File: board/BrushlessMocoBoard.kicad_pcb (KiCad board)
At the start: 2 copper layers, 127 x 127 mm, 116 parts, among them J5 Conn_01x04, Q1 NMOS, Q2 NMOS, Q3 NMOS, Q4 NMOS, Q7 NMOS, Q8 NMOS, SW1 SW_Push, U1 STSPIN32G4TR, U2 SN65HVD232

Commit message: Adjusted diode footprints and grouped layout components
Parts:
- CR1, CR2, CR3, CR4, CR7, CR8: footprint BoCoFootprintLibrary:DO-35_STM -> Diode_THT:D_DO-35_SOD27_P3.81mm_Vertical_KathodeUp
- moved C24 344.5 mm to (267.0, 57.9)
- moved C26 343.5 mm to (251.0, 58.2)
- moved Q3 333.1 mm to (270.2, 70.5)
- moved Q4 333.1 mm to (270.2, 77.2)
- moved R10 313.8 mm to (248.3, 91.5)
- moved R8 313.8 mm to (248.3, 86.4)
- moved R9 313.8 mm to (248.3, 89.0)
- moved C3 313.4 mm to (248.3, 81.9)
- moved TP3 308.8 mm to (257.2, 108.9)
- moved R50 307.6 mm to (259.9, 83.4)
- moved R51 307.6 mm to (259.9, 85.9)
- moved R52 307.6 mm to (259.9, 88.4)
- moved R53 307.6 mm to (259.9, 90.9)
- moved C8 306.7 mm to (229.9, 59.0), turned to 180 degrees
- moved R31 306.5 mm to (249.8, 110.1)
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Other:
- board outline removed

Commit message: Placed some basic planes in the layout and swapped mosfet symbols to match layout footprints.
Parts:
- removed C25, C26: 330 μF, BoCoFootprintLibrary:CAP_PAN_EEE_H13_PAN
- removed CR7, CR8: BAT48, Diode_THT:D_DO-35_SOD27_P3.81mm_Vertical_KathodeUp
- removed Q1, Q2, Q3, Q4, Q7, Q8: NMOS, BoCoFootprintLibrary:PG-TDSON-8_INF
- added C10: 1 µF / 25 V, Capacitor_SMD:C_0603_1608Metric_Pad1.08x0.95mm_HandSolder, F.Cu at (225.0, 72.4)
- added C13 (x2): 10 μF / 25 V, BrushlessMocoBoard:CAPPRD250W45D400H700, F.Cu at (2.89, 2.21)
- added C5: 1 mF, Capacitor_THT:CP_Radial_D12.5mm_P5.00mm, F.Cu at (180.0, 110.6)
- added CR5: BAT48, Diode_THT:D_DO-35_SOD27_P3.81mm_Vertical_KathodeUp, F.Cu at (204.9, 64.1)
- added CR6: BAT48, Diode_THT:D_DO-35_SOD27_P3.81mm_Vertical_KathodeUp, F.Cu at (205.1, 76.2)
- added MOSFET1: BSC035N10NS5ATMA1, BoCoFootprintLibrary:PG-TDSON-8_INF, F.Cu at (120.9, 93.3)
- added MOSFET2: BSC035N10NS5ATMA1, BoCoFootprintLibrary:PG-TDSON-8_INF, F.Cu at (135.9, 93.3)
- added MOSFET3: BSC035N10NS5ATMA1, BoCoFootprintLibrary:PG-TDSON-8_INF, F.Cu at (165.0, 93.7)
- added MOSFET4: BSC035N10NS5ATMA1, BoCoFootprintLibrary:PG-TDSON-8_INF, F.Cu at (180.0, 93.7)
- added MOSFET5: BSC035N10NS5ATMA1, BoCoFootprintLibrary:PG-TDSON-8_INF, F.Cu at (208.9, 93.6)
- added MOSFET6: BSC035N10NS5ATMA1, BoCoFootprintLibrary:PG-TDSON-8_INF, F.Cu at (224.2, 93.6)
- added R11: 47 Ω, Resistor_SMD:R_0603_1608Metric_Pad0.98x0.95mm_HandSolder, F.Cu at (174.6, 80.0)
- added R12: 10 Ω, Resistor_SMD:R_0603_1608Metric_Pad0.98x0.95mm_HandSolder, F.Cu at (168.9, 65.4)
- added R13: 10 Ω, Resistor_SMD:R_0603_1608Metric_Pad0.98x0.95mm_HandSolder, F.Cu at (170.2, 80.0)
- C12: value 1 µF / 25 V -> 1 mF; footprint Capacitor_SMD:C_0603_1608Metric_Pad1.08x0.95mm_HandSolder -> Capacitor_THT:CP_Radial_D12.5mm_P5.00mm
- C24, C8: value 1 mF -> 330 μF; footprint Capacitor_THT:CP_Radial_D12.5mm_P5.00mm -> BoCoFootprintLibrary:CAP_PAN_EEE_H13_PAN
- R43, R50: value 47 Ω -> 1 mΩ / 1%
- R44, R47: value 10 Ω -> 47 Ω
- R46: value 47 Ω -> 10 Ω
- R49: value 1 mΩ / 1% -> 10 Ω
- R51, R52: value 10 Ω -> 0 Ω
- R53: value 1 mΩ / 1% -> 0 Ω
- moved R51 271.9 mm to (1.68, 0.76)
- moved R52 271.9 mm to (1.68, 3.27)
- moved R53 271.9 mm to (1.68, 5.78)
- moved C19 193.5 mm to (168.2, 240.6)
- moved C20 193.5 mm to (172.1, 259.7)
- moved R17 193.5 mm to (172.6, 243.1)
- moved R18 193.5 mm to (167.5, 258.0)
- moved R19 193.5 mm to (167.5, 260.5)
- moved R5 193.5 mm to (163.2, 258.0)
- moved R7 193.5 mm to (163.2, 260.5)
- moved SW1 193.5 mm to (171.2, 247.4)
- moved Conn4 161.9 mm to (57.9, 206.0)
- moved Conn8 161.9 mm to (57.9, 218.1)
- moved TP1 161.1 mm to (320.7, 170.4)
- moved TP4 161.1 mm to (320.8, 177.3)
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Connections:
- C11 pad 2: Vs_U_Low -> GND
- C12 pad 1: /Half-Bridges & Current Sensing/BOOT_V -> 24 V
- C12 pad 2: /Half-Bridges & Current Sensing/OUT_V -> GND
- C14 pad 2: Vs_U_Low -> GND
- C15 pad 2: Vs_U_Low -> GND
- C16 pad 2: Vs_U_Low -> GND
- C17 pad 2: Vs_U_Low -> GND
- C18 pad 2: Vs_U_Low -> GND
- C19 pad 2: Vs_U_Low -> GND
- C2 pad 2: Vs_U_Low -> GND
- C20 pad 2: Vs_U_Low -> GND
- C21 pad 2: Vs_U_Low -> GND
- C22 pad 2: Vs_U_Low -> GND
- C23 pad 2: Vs_U_Low -> GND
- C24 pad 2: Vs_U_Low -> GND
- C3 pad 1: /Half-Bridges & Current Sensing/BOOT_W -> /Half-Bridges & Current Sensing/BOOT_V
- C3 pad 2: /Half-Bridges & Current Sensing/OUT_W -> /Half-Bridges & Current Sensing/OUT_V
- C4 pad 2: Vs_U_Low -> GND
- C6 pad 2: Vs_U_Low -> GND
- C7 pad 2: Vs_U_Low -> GND
- C8 pad 2: Vs_U_Low -> GND
- C9 pad 2: Vs_U_Low -> GND
- CR3 pad 1: /Half-Bridges & Current Sensing/GHS_W -> /Half-Bridges & Current Sensing/GHS_V
- CR3 pad 2: Net-(Q3-G) -> Net-(CR3-Pad2)
- CR4 pad 1: /Half-Bridges & Current Sensing/GLS_W -> /Half-Bridges & Current Sensing/GLS_V
- CR4 pad 2: Net-(Q4-G) -> Net-(CR4-Pad2)
- Conn1 pad 1: Vs_U_Low -> GND
- Conn4 pad 4: Vs_U_Low -> GND
- D1 pad 1: Vs_U_Low -> GND
- D3 pad 1: Vs_U_Low -> GND
- J5 pad 1: +3V3 -> +3.3V
- J5 pad 4: Vs_U_Low -> GND
- R10 pad 1: /Half-Bridges & Current Sensing/GLS_W -> /Half-Bridges & Current Sensing/GLS_V
- R16 pad 2: Vs_U_Low -> GND
- R19 pad 2: Vs_U_Low -> GND
- R22 pad 2: Vs_U_Low -> GND
- R23 pad 2: Vs_U_Low -> GND
- R27 pad 2: Vs_U_Low -> Vs_V_Low
- R29 pad 2: Vs_U_Low -> GND
- R3 pad 2: Vs_U_Low -> GND
- R32 pad 2: Vs_U_Low -> Vs_W_Low
- R34 pad 2: Vs_U_Low -> GND
- R43 pad 1: /Half-Bridges & Current Sensing/GHS_V -> Vs_V_High
- R43 pad 2: Net-(R43-Pad2) -> GND
- R44 pad 1: /Half-Bridges & Current Sensing/GHS_V -> /Half-Bridges & Current Sensing/GHS_W
- R44 pad 2: Net-(R43-Pad2) -> Net-(R44-Pad2)
- R45 pad 1: /Half-Bridges & Current Sensing/GLS_V -> /Half-Bridges & Current Sensing/GHS_W
- R45 pad 2: Net-(R45-Pad2) -> Net-(R44-Pad2)
- R46 pad 1: /Half-Bridges & Current Sensing/GLS_V -> /Half-Bridges & Current Sensing/GLS_W
- R46 pad 2: Net-(R45-Pad2) -> Net-(R46-Pad2)
- R47 pad 1: Net-(R43-Pad2) -> /Half-Bridges & Current Sensing/GLS_W
- R47 pad 2: Net-(Q7-G) -> Net-(R46-Pad2)
- R48 pad 1: Net-(R45-Pad2) -> Net-(R44-Pad2)
- R49 pad 1: Vs_V_High -> Net-(R46-Pad2)
- R49 pad 2: Vs_U_Low -> Net-(CR6-Pad2)
- R50 pad 1: /Half-Bridges & Current Sensing/GLS_W -> Vs_W_High
- R50 pad 2: Net-(R10-Pad2) -> GND
- R51 pad 1: Net-(R51-Pad1) -> GND
- R51 pad 2: Net-(Q3-G) -> Vs_U_Low
- R52 pad 1: Net-(R10-Pad2) -> GND
- R52 pad 2: Net-(Q4-G) -> Vs_V_Low
- R53 pad 1: Vs_W_High -> GND
- R53 pad 2: Vs_U_Low -> Vs_W_Low
- R8 pad 1: /Half-Bridges & Current Sensing/GHS_W -> /Half-Bridges & Current Sensing/GHS_V
- R8 pad 2: Net-(R51-Pad1) -> Net-(R12-Pad1)
- R9 pad 1: /Half-Bridges & Current Sensing/GHS_W -> /Half-Bridges & Current Sensing/GHS_V
- R9 pad 2: Net-(R51-Pad1) -> Net-(R12-Pad1)
- STPS1H100A1 pad 2: Vs_U_Low -> GND
- SW1 pad 1: Vs_U_Low -> GND
- U1 pad 32: Vs_U_Low -> GND
- U1 pad 65: Vs_U_Low -> GND
- U2 pad 2: Vs_U_Low -> GND
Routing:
- added copper zone on B.Cu, net 24 V
- added copper zone on F.Cu, net 24 V
- added copper zone on In1.Cu, net 24 V
- added copper zone on In2.Cu, net 24 V
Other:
- copper layers 2 -> 4

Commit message: Regrouped components on the layout into a rough draft before the next set of zoning and tracing.
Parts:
- removed the C13 at (2.89, 2.21) (x2)
- removed the C13 at (147.7, 32.0)
- removed R51, R52, R53: 0 Ω, Resistor_SMD:R_0603_1608Metric_Pad0.98x0.95mm_HandSolder
- added C13: EEAGA1E100H, BrushlessMocoBoard:CAP_PAN_4X7_PAN, F.Cu at (122.9, 138.3)
- moved Conn9 220.9 mm to (128.5, 93.8), turned to -90 degrees
- moved R24 197.7 mm to (119.2, 125.1)
- moved TP4 197.4 mm to (131.3, 122.1)
- moved R25 197.1 mm to (119.2, 130.1), turned to 180 degrees
- moved R21 194.0 mm to (122.6, 122.0), turned to -90 degrees
- moved R26 191.3 mm to (125.8, 130.1)
- moved R23 190.7 mm to (125.9, 125.1)
- moved TP1 188.0 mm to (137.8, 126.8)
- moved R36 187.2 mm to (130.9, 130.1)
- moved R27 185.4 mm to (153.7, 130.0), turned to 180 degrees
- moved R20 185.2 mm to (153.6, 125.1)
- moved R28 185.1 mm to (157.0, 121.9), turned to -90 degrees
- moved R29 181.8 mm to (160.3, 125.1)
- moved TP5 179.9 mm to (165.8, 122.0)
- moved R30 178.3 mm to (160.3, 130.0)
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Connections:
- R18 pad 1: VM -> 24 V
- R5 pad 1: VM -> 24 V

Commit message: Significant progress on board layout. Added GPIO and UART pins, also rearranged encoder and I2C MCU pins.
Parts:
- added J1: Conn_01x04, Connector_PinSocket_2.54mm:PinSocket_1x04_P2.54mm_Vertical, F.Cu at (130.0, 58.4)
- added J2: Conn_02x06_Odd_Even, Connector_PinSocket_2.54mm:PinSocket_2x06_P2.54mm_Vertical, F.Cu at (125.4, 58.4)
- added R51: 0 Ω, Resistor_SMD:R_0603_1608Metric_Pad0.98x0.95mm_HandSolder, F.Cu at (136.5, 57.4)
- added R52: 0 Ω, Resistor_SMD:R_0603_1608Metric_Pad0.98x0.95mm_HandSolder, F.Cu at (136.5, 59.9)
- added R53: 0 Ω, Resistor_SMD:R_0603_1608Metric_Pad0.98x0.95mm_HandSolder, F.Cu at (136.5, 62.4)
- added R54: 100 kΩ / 5 %, Resistor_SMD:R_0603_1608Metric_Pad0.98x0.95mm_HandSolder, F.Cu at (136.5, 66.9)
- CR1, CR2, CR3, CR4, CR5, CR6, MOSFET1, MOSFET2, MOSFET3, MOSFET4, MOSFET5, MOSFET6, R1, R10, R11, R12, R13, R2, R20, R21, R23, R24, R25, R26, R27, R28, R29, R3, R30, R31, R32, R33, R34, R35, R36, R37, R38, R39, R40, R41, R42, R43, R44, R45, R46, R47, R48, R49, R50, R8, R9, TP1, TP2, TP3, TP4, TP5, TP6: moved to B.Cu
- moved H1 391.2 mm to (33.7, 36.9)
- moved H4 360.7 mm to (33.7, 123.4)
- moved H2 314.2 mm to (136.3, 36.9)
- moved H3 275.8 mm to (136.3, 123.3)
- moved CR5 152.6 mm to (96.8, 39.6), turned to 90 degrees
- moved R44 151.6 mm to (100.6, 41.3), turned to 90 degrees
- moved R45 150.0 mm to (103.8, 41.3), turned to 90 degrees
- moved R48 147.7 mm to (103.8, 36.3), turned to 90 degrees
- moved CR6 147.2 mm to (108.4, 39.6), turned to 90 degrees
- moved R47 146.3 mm to (112.2, 41.3), turned to 90 degrees
- moved R46 145.2 mm to (115.3, 41.3), turned to 90 degrees
- moved R49 143.6 mm to (115.3, 36.3), turned to 90 degrees
- moved C19 139.3 mm to (99.1, 104.6)
- moved C21 139.3 mm to (103.9, 105.1)
- moved D1 139.3 mm to (116.1, 104.1)
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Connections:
- U1 pad 12: unconnected-(U1-PC3-Pad12) -> /MCU/I/O_PC3
- U1 pad 17: unconnected-(U1-PA4-Pad17) -> /MCU/I/O_PA4
- U1 pad 22: unconnected-(U1-PC5-Pad22) -> /MCU/I/O_PC5
- U1 pad 28: /Interfaces/ENC_A/PWM -> /MCU/I/O_PB10
- U1 pad 3: unconnected-(U1-PC13-Pad3) -> Net-(U1-PC13)
- U1 pad 4: unconnected-(U1-PC14-Pad4) -> /MCU/I/O_PC14
- U1 pad 44: unconnected-(U1-PA8-Pad44) -> /MCU/I/O_PA8
- U1 pad 45: unconnected-(U1-PA9-Pad45) -> /MCU/UART_TX
- U1 pad 46: unconnected-(U1-PA10-Pad46) -> /MCU/UART_RX
- U1 pad 5: unconnected-(U1-PC15-Pad5) -> /MCU/I/O_PC15
- U1 pad 51: /Interfaces/ENC_B -> /MCU/I/O_PA15
- U1 pad 53: unconnected-(U1-PD2-Pad53) -> /MCU/I/O_PD2
- U1 pad 54: unconnected-(U1-PB3-Pad54) -> /MCU/I/O_PB3
- U1 pad 55: unconnected-(U1-PB4-Pad55) -> /MCU/I/O_PB4
- U1 pad 56: unconnected-(U1-PB5-Pad56) -> /MCU/I/O_PB5
- U1 pad 57: unconnected-(U1-PB6-Pad57) -> /Interfaces/ENC_A/PWM
- U1 pad 58: /Interfaces/I2C1_SDA -> /Interfaces/ENC_B
- U1 pad 60: unconnected-(U1-PB9-Pad60) -> /Interfaces/I2C1_SDA
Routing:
- added copper zone on B.Cu, net /Half-Bridges & Current Sensing/OUT_U
- added copper zone on F.Cu, net /Half-Bridges & Current Sensing/OUT_U
- added copper zone on In1.Cu, net /Half-Bridges & Current Sensing/OUT_U
- added copper zone on In2.Cu, net /Half-Bridges & Current Sensing/OUT_U
- added copper zone on B.Cu, net /Half-Bridges & Current Sensing/OUT_V
- added copper zone on F.Cu, net /Half-Bridges & Current Sensing/OUT_V
- added copper zone on In1.Cu, net /Half-Bridges & Current Sensing/OUT_V
- added copper zone on In2.Cu, net /Half-Bridges & Current Sensing/OUT_V
- added copper zone on B.Cu, net /Half-Bridges & Current Sensing/OUT_W
- added copper zone on F.Cu, net /Half-Bridges & Current Sensing/OUT_W
- added copper zone on In1.Cu, net /Half-Bridges & Current Sensing/OUT_W
- added copper zone on In2.Cu, net /Half-Bridges & Current Sensing/OUT_W
- added copper zone on B.Cu, net GND

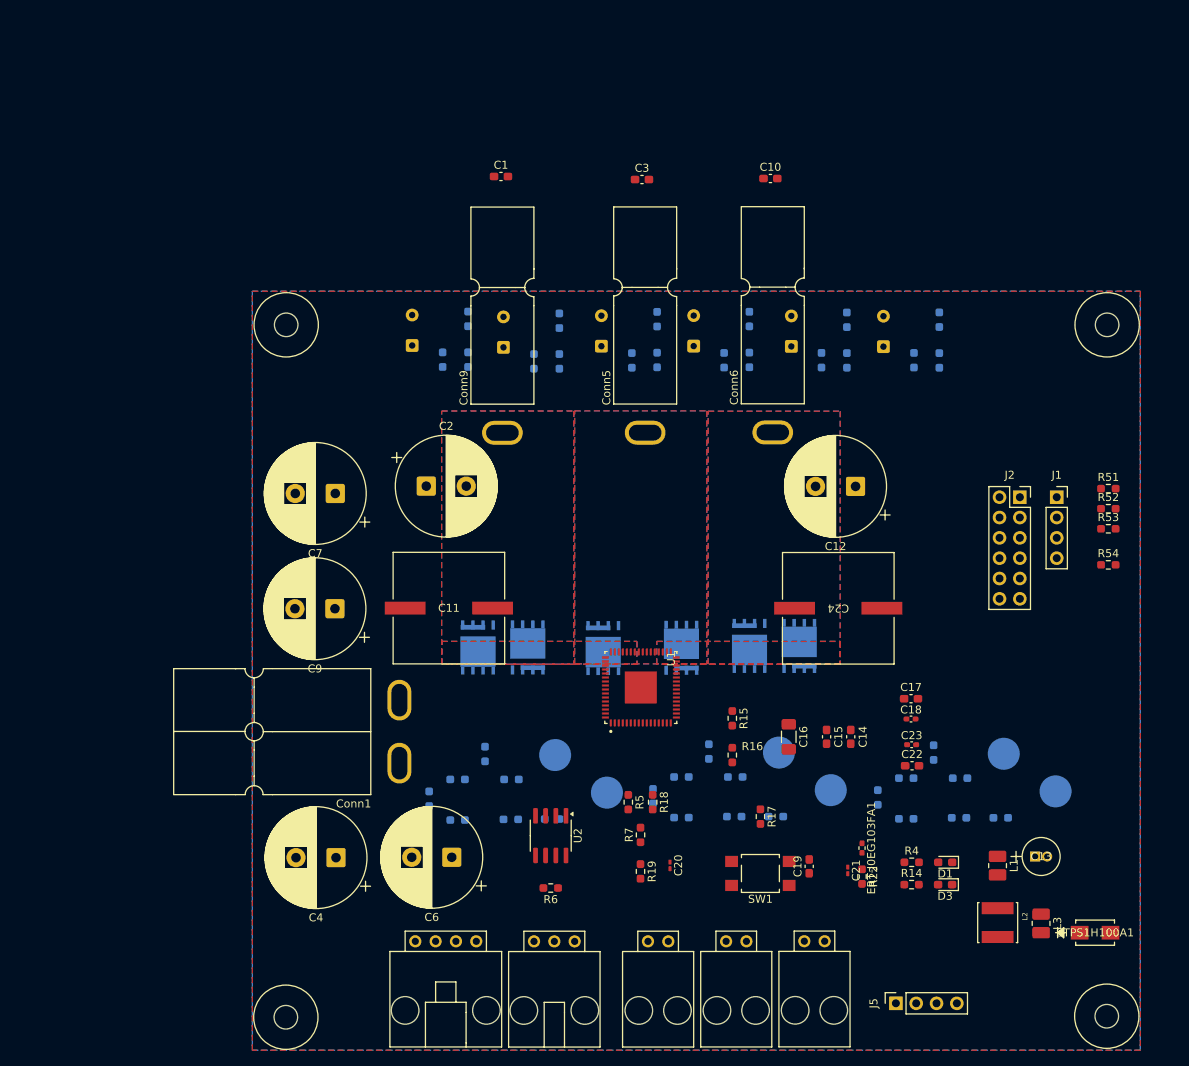
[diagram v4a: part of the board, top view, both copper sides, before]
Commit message: Rearranged components on the layout, added a switch, and connected hierarchical labels in the schematic.
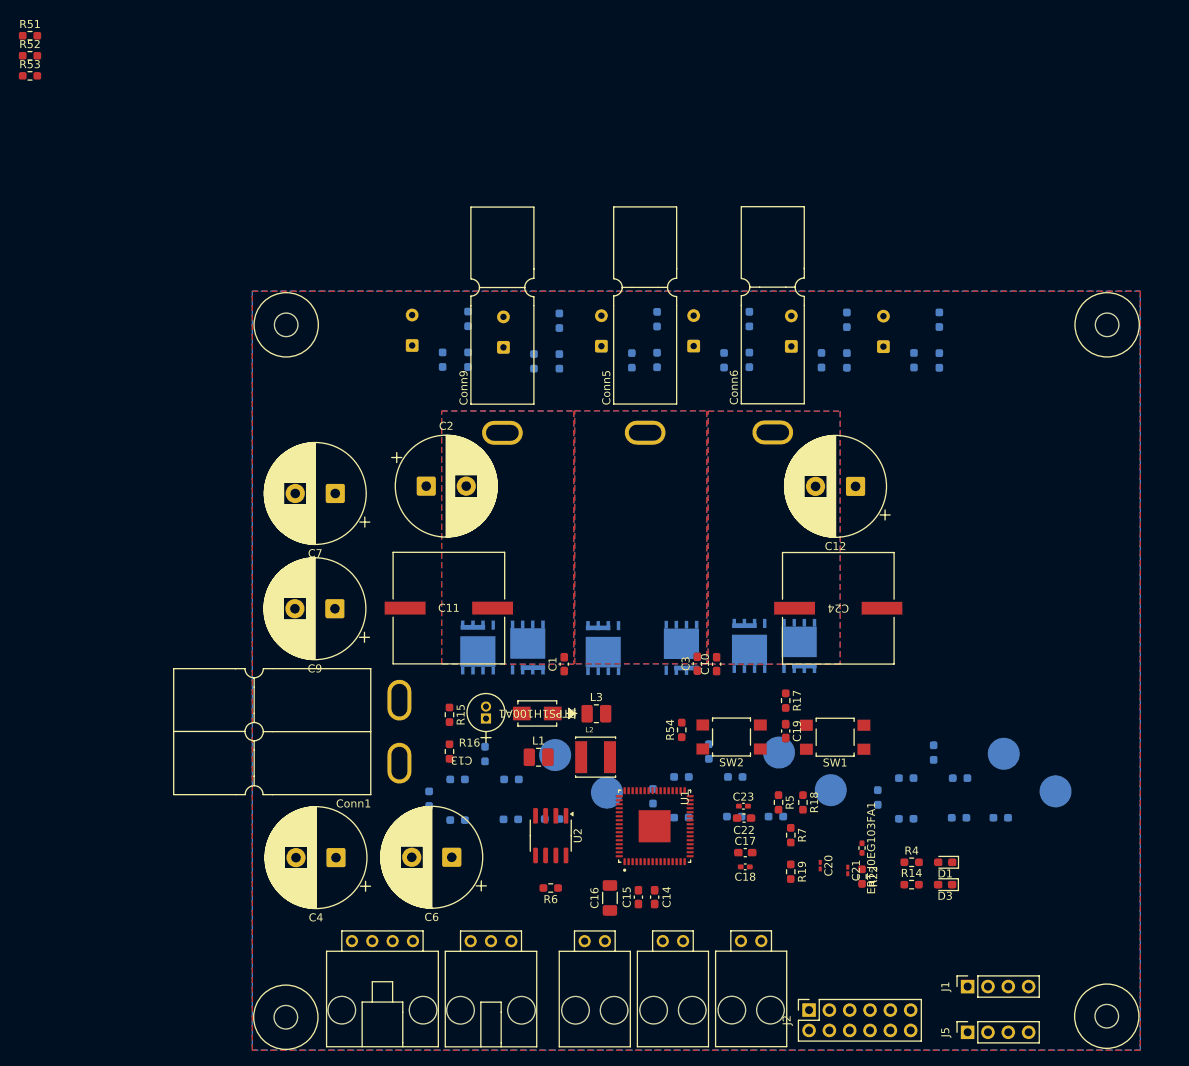
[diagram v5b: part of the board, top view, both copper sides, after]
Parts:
- added SW2: SW_Push, MRDT_Switches:SW_SPST_TL3305A, F.Cu at (89.4, 88.4)
- moved R51 146.2 mm to (1.68, 0.76)
- moved R52 146.2 mm to (1.68, 3.27)
- moved R53 146.2 mm to (1.68, 5.78)
- moved STPS1H100A1 74.9 mm to (65.1, 85.5), turned to 180 degrees
- moved C13 70.8 mm to (58.7, 86.1), turned to 90 degrees
- moved J2 69.3 mm to (99.1, 122.6), turned to 90 degrees
- moved J1 62.2 mm to (118.9, 119.6), turned to 90 degrees
- moved C1 61.5 mm to (68.5, 79.3), turned to 90 degrees
- moved L3 61.5 mm to (72.5, 85.5), turned to 0 degrees
- moved C10 61.1 mm to (87.5, 79.3), turned to 90 degrees
- moved C3 60.9 mm to (85.1, 79.2), turned to 90 degrees
- moved L1 58.9 mm to (65.3, 90.9), turned to 0 degrees
- moved R54 57.2 mm to (83.1, 87.5), turned to 90 degrees
- moved L2 54.4 mm to (72.4, 90.9), turned to 0 degrees
- moved R15 35.4 mm to (54.1, 85.6)
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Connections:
- U1 pad 12: /MCU/I/O_PC3 -> /Interfaces/I/O_PC3
- U1 pad 17: /MCU/I/O_PA4 -> /Interfaces/I/O_PA4
- U1 pad 22: /MCU/I/O_PC5 -> /Interfaces/I/O_PC5
- U1 pad 28: /MCU/I/O_PB10 -> /Interfaces/I/O_PB10
- U1 pad 4: /MCU/I/O_PC14 -> /Interfaces/I/O_PC14
- U1 pad 44: /MCU/I/O_PA8 -> /Interfaces/I/O_PA8
- U1 pad 45: /MCU/UART_TX -> /Interfaces/UART_TX
- U1 pad 46: /MCU/UART_RX -> /Interfaces/UART_RX
- U1 pad 5: /MCU/I/O_PC15 -> /Interfaces/I/O_PC15
- U1 pad 51: /MCU/I/O_PA15 -> /Interfaces/I/O_PA15
- U1 pad 53: /MCU/I/O_PD2 -> /Interfaces/I/O_PD2
- U1 pad 54: /MCU/I/O_PB3 -> /Interfaces/I/O_PB3
- U1 pad 55: /MCU/I/O_PB4 -> /Interfaces/I/O_PB4
- U1 pad 56: /MCU/I/O_PB5 -> /Interfaces/I/O_PB5

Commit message: Made layout adjustments according to board review.
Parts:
- removed C11, C24, C8: 330 μF, BoCoFootprintLibrary:CAP_PAN_EEE_H13_PAN
- removed C12, C2, C5: 1 mF, Capacitor_THT:CP_Radial_D12.5mm_P5.00mm
- removed CR1, CR2, CR3, CR4, CR5, CR6: BAT48, Diode_THT:D_DO-35_SOD27_P3.81mm_Vertical_KathodeUp
- removed J1, J5: Conn_01x04, Connector_PinSocket_2.54mm:PinSocket_1x04_P2.54mm_Vertical
- removed J2: Conn_02x06_Odd_Even, Connector_PinSocket_2.54mm:PinSocket_2x06_P2.54mm_Vertical
- removed R51, R52, R53: 0 Ω, Resistor_SMD:R_0603_1608Metric_Pad0.98x0.95mm_HandSolder
- removed TP1, TP2, TP3, TP4, TP5, TP6: TestPoint, TestPoint:TestPoint_Pad_D4.0mm
- added Conn10: Molex_SL_04, MRDT_Connectors:MOLEX_SL_04_Vertical, F.Cu at (42.4, 44.7)
- added Conn11: Molex_SL_04, MRDT_Connectors:MOLEX_SL_04_Vertical, F.Cu at (55.9, 44.7)
- added Conn12: Molex_SL_06, MRDT_Connectors:MOLEX_SL_06_Vertical, F.Cu at (133.2, 84.8)
- added Conn13: Molex_SL_06, MRDT_Connectors:MOLEX_SL_06_Vertical, F.Cu at (133.2, 103.1)
- added Conn14: Molex_SL_03, MRDT_Connectors:MOLEX_SL_03_Vertical, F.Cu at (47.1, 122.9)
- added Conn15: Molex_SL_03, MRDT_Connectors:MOLEX_SL_03_Vertical, F.Cu at (57.9, 122.9)
- added Conn16: Molex_SL_03, MRDT_Connectors:MOLEX_SL_03_Vertical, F.Cu at (68.7, 122.9)
- added D2: D_Schottky, Diode_SMD:D_SOD-123, B.Cu at (79.3, 77.7)
- added D4: D_Schottky, Diode_SMD:D_SOD-123, B.Cu at (86.3, 77.7)
- added D5: D_Schottky, Diode_SMD:D_SOD-123, B.Cu at (96.0, 77.7)
- added D6: D_Schottky, Diode_SMD:D_SOD-123, B.Cu at (112.6, 77.6)
- added D7: D_Schottky, Diode_SMD:D_SOD-123, B.Cu at (102.9, 77.7)
- added D8: D_Schottky, Diode_SMD:D_SOD-123, B.Cu at (119.6, 77.6)
- added NT1: NetTie_2, NetTie:NetTie-2_SMD_Pad0.5mm, B.Cu at (105.5, 85.4)
- added NT2: NetTie_2, NetTie:NetTie-2_SMD_Pad0.5mm, B.Cu at (88.8, 85.4)
- added NT3: NetTie_2, NetTie:NetTie-2_SMD_Pad0.5mm, B.Cu at (72.2, 85.4)
- C1, C10, C3: moved to B.Cu
- C20, C21: footprint Capacitor_SMD:C_0201_0603Metric_Pad0.64x0.40mm_HandSolder -> Capacitor_SMD:C_0603_1608Metric_Pad1.08x0.95mm_HandSolder
- Conn2, Conn3, Conn7: footprint MRDT_Connectors:MOLEX_SL_02_Horizontal -> MRDT_Connectors:MOLEX_SL_02_Vertical
- Conn4: footprint MRDT_Connectors:MOLEX_SL_04_Horizontal -> MRDT_Connectors:MOLEX_SL_04_Vertical
- Conn8: footprint MRDT_Connectors:MOLEX_SL_03_Horizontal -> MRDT_Connectors:MOLEX_SL_03_Vertical
- moved Conn7 73.4 mm to (69.3, 44.4), turned to 0 degrees
- moved Conn3 71.3 mm to (34.1, 54.6), turned to 90 degrees
- moved Conn2 70.9 mm to (34.2, 62.9), turned to 90 degrees
- moved R15 60.0 mm to (102.1, 121.7), turned to 180 degrees
- moved R16 54.2 mm to (98.3, 121.7), turned to 180 degrees
- moved R6 53.7 mm to (39.2, 61.2), turned to 90 degrees
- moved R54 50.1 mm to (131.7, 75.3), turned to 180 degrees
- moved R39 48.1 mm to (81.9, 80.0)
- moved R1 47.5 mm to (83.9, 80.0)
- moved R40 47.4 mm to (81.9, 76.2)
- moved SW2 47.3 mm to (132.6, 69.2), turned to -90 degrees
- moved R41 45.5 mm to (88.8, 80.0)
- moved R42 45.0 mm to (88.8, 76.2)
- moved R2 44.9 mm to (90.9, 80.0)
- moved U2 44.8 mm to (45.7, 61.2), turned to 180 degrees
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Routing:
- added copper zone on F.Cu, net +3.3V
- added copper zone on B.Cu, net Net-(L1-Pad2)
- added copper zone on F.Cu, net Net-(L1-Pad2)
- added copper zone on In1.Cu, net Net-(L1-Pad2)
- added copper zone on In2.Cu, net Net-(L1-Pad2)
- added copper zone on B.Cu, net Net-(U1-REGIN)
- added copper zone on F.Cu, net Net-(U1-REGIN)
- added copper zone on In1.Cu, net Net-(U1-REGIN)
- added copper zone on In2.Cu, net Net-(U1-REGIN)
- added copper zone on B.Cu, net Net-(U1-SW)
- added copper zone on F.Cu, net Net-(U1-SW)
- added copper zone on In1.Cu, net Net-(U1-SW)
- added copper zone on In2.Cu, net Net-(U1-SW)

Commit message: Fixed footprint and symbol for FETs
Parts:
- moved H4 0.25 mm to (33.9, 123.4)
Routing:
- net GND: vias 0 -> 1
